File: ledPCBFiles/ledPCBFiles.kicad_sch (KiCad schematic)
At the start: 0 parts

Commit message: Added 555 timer
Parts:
- added R1: 10k, symbol Device:R
- added U1: LM555xN, Package_DIP:DIP-8_W7.62mm, symbol Timer:LM555xN
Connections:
- new net +6V: U1.8 (VCC)
- new net GND: U1.1 (GND)
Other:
- title: (none) -> Schematic for 4-Bit LED Counter

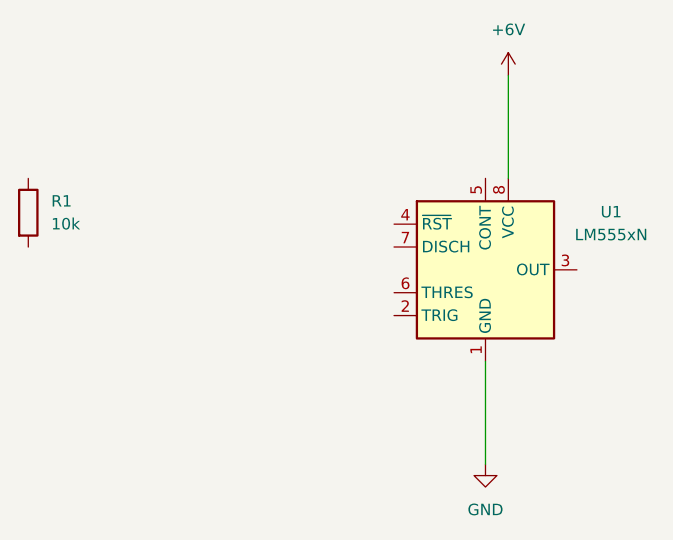
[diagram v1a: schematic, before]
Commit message: Added 100 nF capacitor to pin 5 on 555 timer
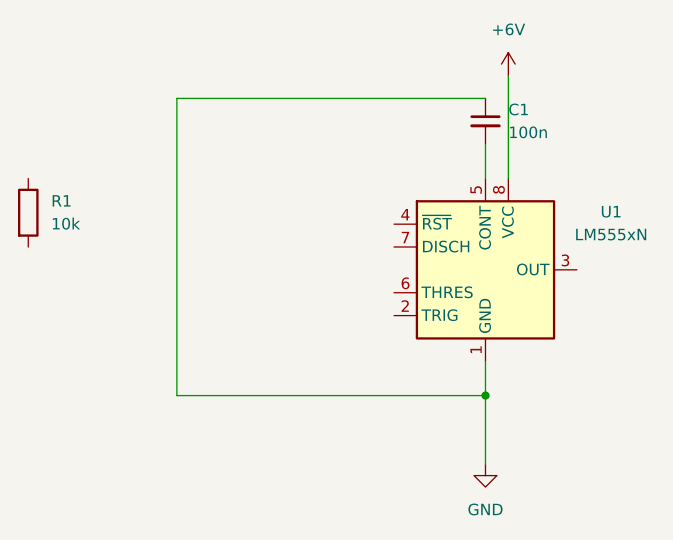
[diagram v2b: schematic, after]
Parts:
- added C1: 100n, symbol Device:C_Small
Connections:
- net GND: now also C1.1
- net at U1.5 (CONT): now also C1.2
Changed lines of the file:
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@@
 		(date "2026-06-07")
 	)
-	(wire
-		(pts
-			(xy 119.38 93.98) (xy 119.38 105.41)
+	(junction
+		(at 119.38 97.79)
+		(diameter 0)
+		(color 0 0 0 0)
+	)
+	(wire
+		(pts
+			(xy 119.38 97.79) (xy 119.38 105.41)
+		)
+		(stroke
+			(width 0)
+			(type default)
+		)
+	)
+	(wire
+		(pts
+			(xy 85.09 97.79) (xy 119.38 97.79)
+		)
+		(stroke
+			(width 0)
+			(type default)
+		)
+	)
+	(wire
+		(pts
+			(xy 85.09 64.77) (xy 85.09 97.79)
+		)
+		(stroke
+			(width 0)
+			(type default)
+		)
+	)
+	(wire
+		(pts
+			(xy 119.38 64.77) (xy 85.09 64.77)
+		)
+		(stroke
+			(width 0)
+			(type default)
+		)
+	)
+	(wire
+		(pts
+			(xy 119.38 69.85) (xy 119.38 73.66)
+		)
+		(stroke
+			(width 0)
+			(type default)
+		)
+	)
+	(wire
+		(pts
+			(xy 119.38 93.98) (xy 119.38 97.79)
 		)
 		(stroke
@@
 					(unit 1)
 				)
+			)
+		)
+	)
+	(symbol
+		(lib_id "Device:C_Small")
+		(at 119.38 67.31 0)
+		(unit 1)
+		(body_style 1)
+		(exclude_from_sim no)
+		(in_bom yes)
+		(on_board yes)
+		(in_pos_files yes)
+		(dnp no)
+		(fields_autoplaced yes)
+		(property "Reference" "C1"
+			(at 121.92 66.0462 0)
+			(show_name no)
+			(do_not_autoplace no)
+			(effects
+				(font
+					(size 1.27 1.27)
+				)
+				(justify left)
+			)
+		)
+		(property "Value" "100n"
+			(at 121.92 68.5862 0)
+			(show_name no)
+			(do_not_autoplace no)
+			(effects
+				(font
+					(size 1.27 1.27)
+				)
+				(justify left)
+			)
+		)
+		(property "Footprint" ""
+			(at 119.38 67.31 0)
+			(hide yes)
+			(show_name no)
+			(do_not_autoplace no)
+			(effects
+				(font
+					(size 1.27 1.27)
+				)
+			)
+		)
+		(property "Datasheet" ""
+			(at 119.38 67.31 0)
+			(hide yes)
+			(show_name no)
+			(do_not_autoplace no)
+			(effects
+				(font
+					(size 1.27 1.27)
+				)
+			)
+		)
+		(property "Description" "Unpolarized capacitor, small symbol"
+			(at 119.38 67.31 0)
+			(hide yes)
+			(show_name no)
+			(do_not_autoplace no)
+			(effects
+				(font
+					(size 1.27 1.27)
+				)
+			)
+		)
+		(pin "2"
+		)
+		(pin "1"
+		)
+		(instances
+			(project "ledPCBFiles"
+				(path "/4f60fb88-ed3b-40be-bc71-757dad150f17"
+					(reference "C1")
+					(unit 1)
+				)

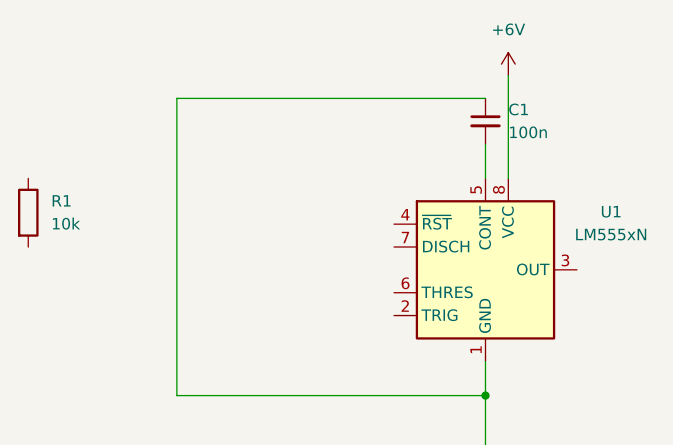
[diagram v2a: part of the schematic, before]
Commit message: Added a resistor
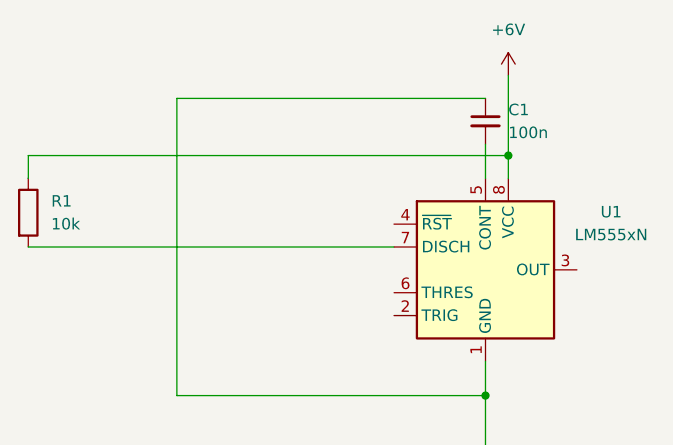
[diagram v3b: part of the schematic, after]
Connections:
- net +6V: now also R1.1
- net at U1.7 (DISCH): now also R1.2
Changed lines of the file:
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@@
+	)
+	(junction
+		(at 121.92 71.12)
+		(diameter 0)
+		(color 0 0 0 0)
 	)
 	(junction
@@
 		(diameter 0)
 		(color 0 0 0 0)
+	)
+	(wire
+		(pts
+			(xy 68.58 81.28) (xy 109.22 81.28)
+		)
+		(stroke
+			(width 0)
+			(type default)
+		)
 	)
 	(wire
@@
 		(pts
 			(xy 85.09 97.79) (xy 119.38 97.79)
+		)
+		(stroke
+			(width 0)
+			(type default)
+		)
+	)
+	(wire
+		(pts
+			(xy 68.58 73.66) (xy 68.58 71.12)
 		)
 		(stroke
@@
 	(wire
 		(pts
-			(xy 121.92 62.23) (xy 121.92 73.66)
+			(xy 68.58 71.12) (xy 121.92 71.12)
 		)
 		(stroke
+			(width 0)
+			(type default)
+		)
+	)
+	(wire
+		(pts
+			(xy 121.92 62.23) (xy 121.92 71.12)
+		)
+		(stroke
+			(width 0)
+			(type default)
+		)
+	)
+	(wire
+		(pts
+			(xy 121.92 71.12) (xy 121.92 73.66)
+		)
+		(stroke

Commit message: Removed resistor
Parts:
- removed R1: 10k, symbol Device:R
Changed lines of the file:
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@@
-	)
-	(junction
-		(at 121.92 71.12)
-		(diameter 0)
-		(color 0 0 0 0)
 	)
 	(junction
@@
 		(diameter 0)
 		(color 0 0 0 0)
-	)
-	(wire
-		(pts
-			(xy 68.58 81.28) (xy 109.22 81.28)
-		)
-		(stroke
-			(width 0)
-			(type default)
-		)
 	)
 	(wire
@@
 		(pts
 			(xy 85.09 97.79) (xy 119.38 97.79)
-		)
-		(stroke
-			(width 0)
-			(type default)
-		)
-	)
-	(wire
-		(pts
-			(xy 68.58 73.66) (xy 68.58 71.12)
 		)
 		(stroke
@@
 	(wire
 		(pts
-			(xy 68.58 71.12) (xy 121.92 71.12)
-		)
-		(stroke
-			(width 0)
-			(type default)
-		)
-	)
-	(wire
-		(pts
-			(xy 121.92 62.23) (xy 121.92 71.12)
-		)
-		(stroke
-			(width 0)
-			(type default)
-		)
-	)
-	(wire
-		(pts
-			(xy 121.92 71.12) (xy 121.92 73.66)
+			(xy 121.92 62.23) (xy 121.92 73.66)
 		)
 		(stroke
@@
 					(unit 1)
 				)
-			)
-		)
-	)
-	(symbol
-		(lib_id "Device:R")
-		(at 68.58 77.47 0)
-		(unit 1)
-		(body_style 1)
-		(exclude_from_sim no)
-		(in_bom yes)
-		(on_board yes)
-		(in_pos_files yes)
-		(dnp no)
-		(fields_autoplaced yes)
-		(property "Reference" "R1"
-			(at 71.12 76.1999 0)
-			(show_name no)
-			(do_not_autoplace no)
-			(effects
-				(font
-					(size 1.27 1.27)
-				)
-				(justify left)
-			)
-		)
-		(property "Value" "10k"
-			(at 71.12 78.7399 0)
-			(show_name no)
-			(do_not_autoplace no)
-			(effects
-				(font
-					(size 1.27 1.27)
-				)
-				(justify left)
-			)
-		)
-		(property "Footprint" ""
-			(at 66.802 77.47 90)
-			(hide yes)
-			(show_name no)
-			(do_not_autoplace no)
-			(effects
-				(font
-					(size 1.27 1.27)
-				)
-			)
-		)
-		(property "Datasheet" ""
-			(at 68.58 77.47 0)
-			(hide yes)
-			(show_name no)
-			(do_not_autoplace no)
-			(effects
-				(font
-					(size 1.27 1.27)
-				)
-			)
-		)
-		(property "Description" "Resistor"
-			(at 68.58 77.47 0)
-			(hide yes)
-			(show_name no)
-			(do_not_autoplace no)
-			(effects
-				(font
-					(size 1.27 1.27)
-				)
-			)
-		)
-		(pin "2"
-		)
-		(pin "1"
-		)
-		(instances
-			(project "ledPCBFiles"
-				(path "/4f60fb88-ed3b-40be-bc71-757dad150f17"
-					(reference "R1")
-					(unit 1)
-				)

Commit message: added a resistor
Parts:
- added R1: 10k, symbol Device:R_US
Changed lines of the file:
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@@
+	)
+	(symbol
+		(lib_id "Device:R_US")
+		(at 69.85 76.2 0)
+		(unit 1)
+		(body_style 1)
+		(exclude_from_sim no)
+		(in_bom yes)
+		(on_board yes)
+		(in_pos_files yes)
+		(dnp no)
+		(fields_autoplaced yes)
+		(property "Reference" "R1"
+			(at 72.39 74.9299 0)
+			(show_name no)
+			(do_not_autoplace no)
+			(effects
+				(font
+					(size 1.27 1.27)
+				)
+				(justify left)
+			)
+		)
+		(property "Value" "10k"
+			(at 72.39 77.4699 0)
+			(show_name no)
+			(do_not_autoplace no)
+			(effects
+				(font
+					(size 1.27 1.27)
+				)
+				(justify left)
+			)
+		)
+		(property "Footprint" ""
+			(at 70.866 76.454 90)
+			(hide yes)
+			(show_name no)
+			(do_not_autoplace no)
+			(effects
+				(font
+					(size 1.27 1.27)
+				)
+			)
+		)
+		(property "Datasheet" ""
+			(at 69.85 76.2 0)
+			(hide yes)
+			(show_name no)
+			(do_not_autoplace no)
+			(effects
+				(font
+					(size 1.27 1.27)
+				)
+			)
+		)
+		(property "Description" "Resistor, US symbol"
+			(at 69.85 76.2 0)
+			(hide yes)
+			(show_name no)
+			(do_not_autoplace no)
+			(effects
+				(font
+					(size 1.27 1.27)
+				)
+			)
+		)
+		(pin "1"
+		)
+		(pin "2"
+		)
+		(instances
+			(project "ledPCBFiles"
+				(path "/4f60fb88-ed3b-40be-bc71-757dad150f17"
+					(reference "R1")
+					(unit 1)
+				)
+			)
+		)
 	)
 	(symbol

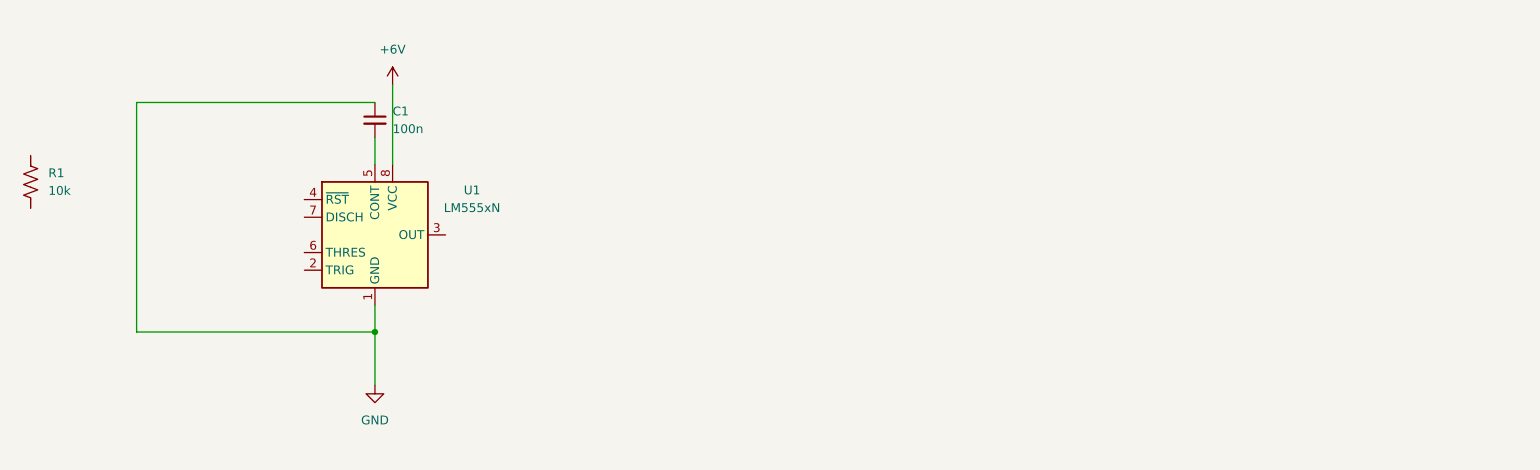
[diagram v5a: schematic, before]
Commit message: Added resistors and LEDs to 74LS161 counter
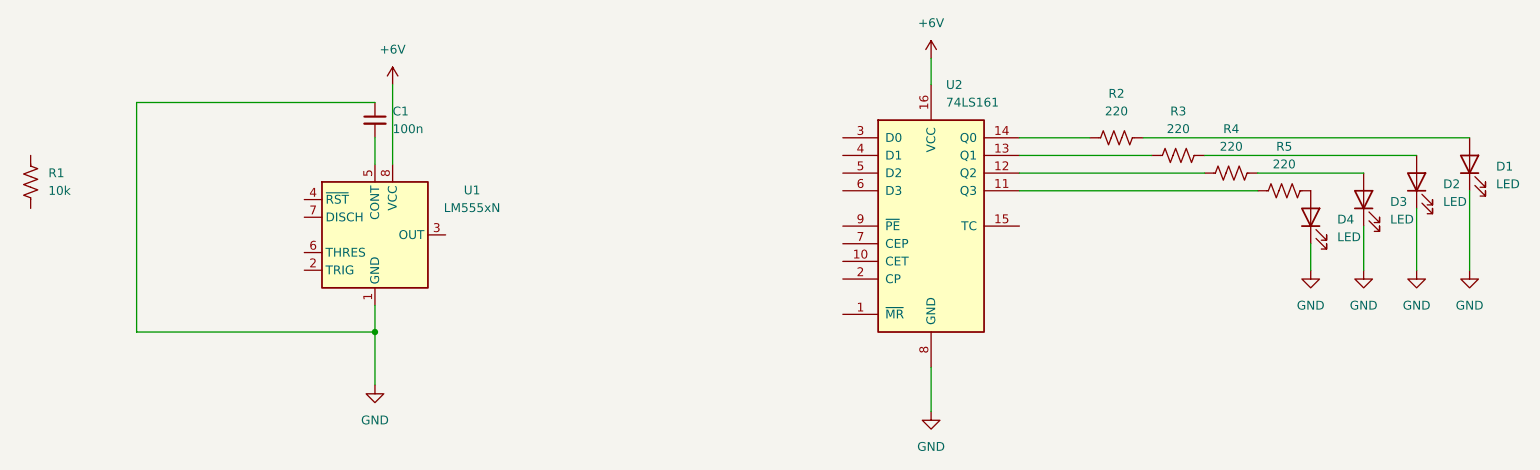
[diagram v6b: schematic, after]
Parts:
- added D1, D2, D3, D4: LED, symbol Device:LED
- added R2, R3, R4, R5: 220, symbol Device:R_US
- added U2: 74LS161, symbol 74xx:74LS161
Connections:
- net +6V: now also U2.16 (VCC)
- net GND: now also D1.1 (K), D2.1 (K), D3.1 (K), D4.1 (K), U2.8 (GND)
- new net: D3.2 (A), R4.2
- new net: R4.1, U2.12 (Q2)
- new net: D1.2 (A), R2.2
- new net: D2.2 (A), R3.2
- new net: R2.1, U2.14 (Q0)
- new net: R5.1, U2.11 (Q3)
- new net: D4.2 (A), R5.2
- new net: R3.1, U2.13 (Q1)

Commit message: Added voltages to counter
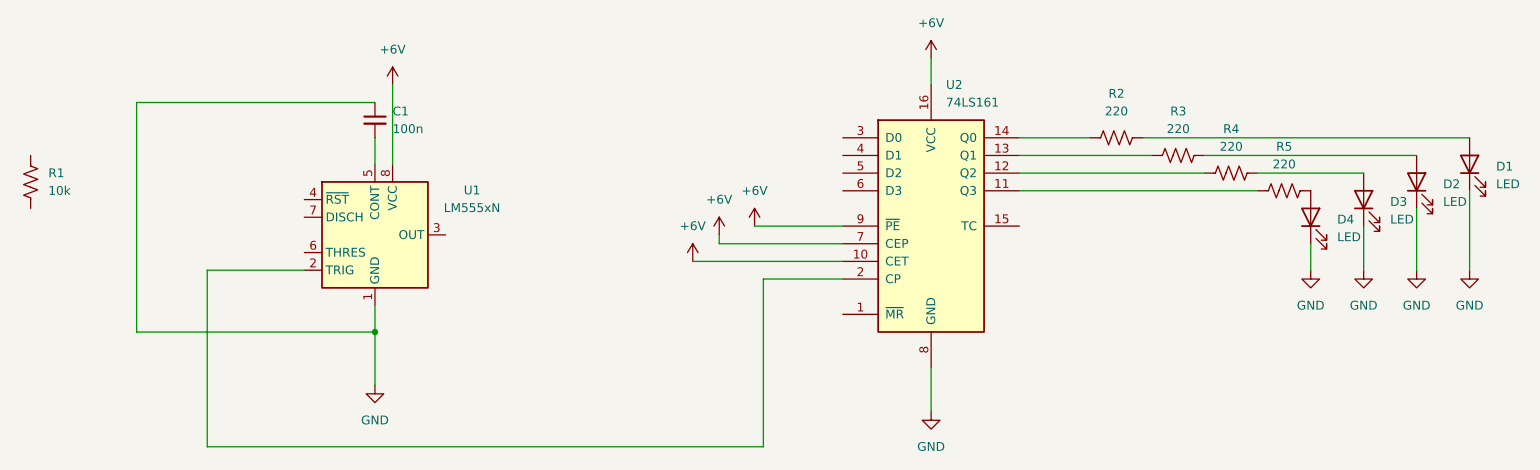
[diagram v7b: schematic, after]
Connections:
- net +6V: now also U2.10 (CET), U2.7 (CEP), U2.9 (~{PE})
- net at U1.2 (TRIG): now also U2.2 (CP)

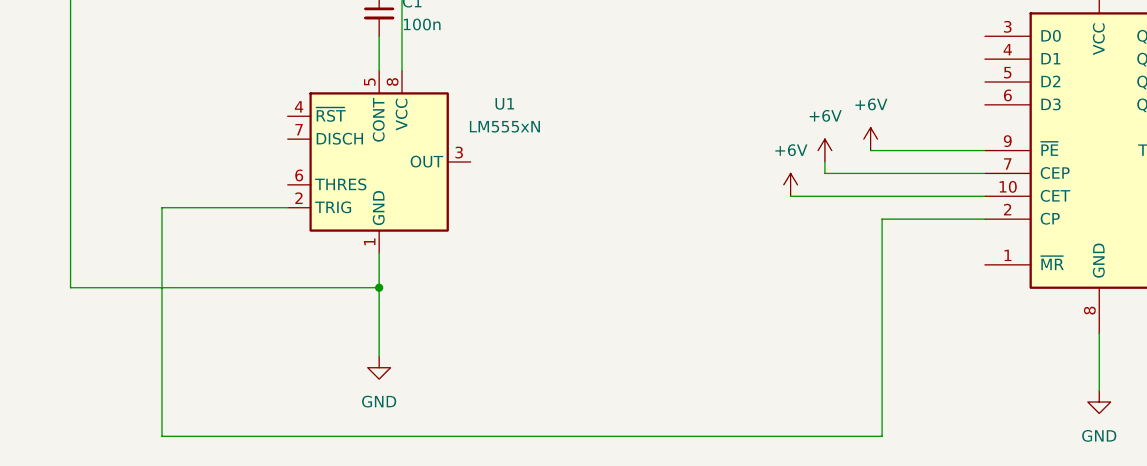
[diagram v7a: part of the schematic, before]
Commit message: Changes connection from pin 3 on 555 timer to pin 2 on 74LS161
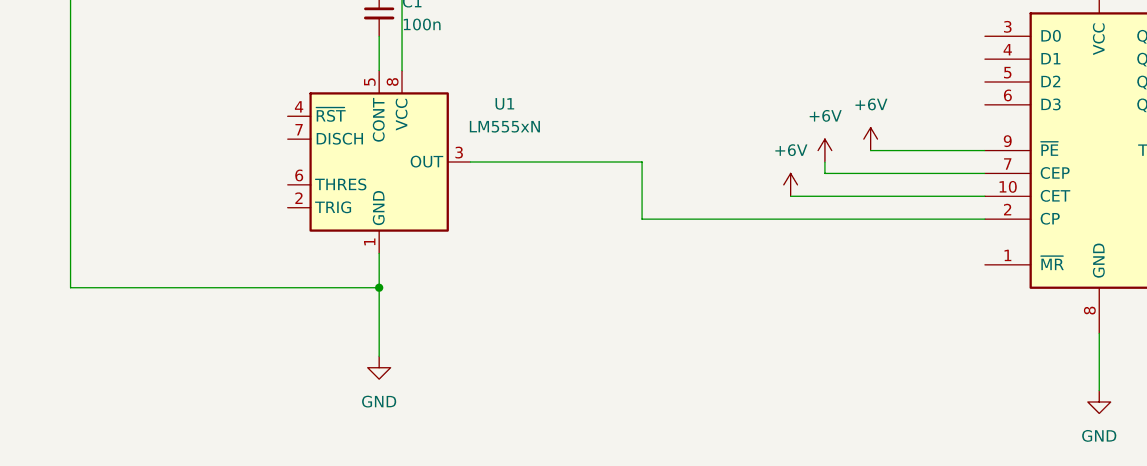
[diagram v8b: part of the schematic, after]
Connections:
- net at U1.2 (TRIG): no longer U2.2 (CP)
- net at U1.3 (OUT): now also U2.2 (CP)
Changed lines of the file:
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@@
-	(wire
-		(pts
-			(xy 95.25 88.9) (xy 95.25 114.3)
-		)
-		(stroke
-			(width 0)
-			(type default)
-		)
-	)
-	(wire
-		(pts
-			(xy 95.25 114.3) (xy 175.26 114.3)
-		)
-		(stroke
-			(width 0)
-			(type default)
-		)
-	)
-	(wire
-		(pts
-			(xy 175.26 90.17) (xy 186.69 90.17)
-		)
-		(stroke
-			(width 0)
-			(type default)
-		)
-	)
 	(wire
 		(pts
@@
 	(wire
 		(pts
+			(xy 129.54 83.82) (xy 148.59 83.82)
+		)
+		(stroke
+			(width 0)
+			(type default)
+		)
+	)
+	(wire
+		(pts
 			(xy 269.24 80.01) (xy 269.24 88.9)
 		)
@@
 	(wire
 		(pts
-			(xy 109.22 88.9) (xy 95.25 88.9)
+			(xy 148.59 90.17) (xy 186.69 90.17)
+		)
+		(stroke
+			(width 0)
+			(type default)
+		)
+	)
+	(wire
+		(pts
+			(xy 148.59 83.82) (xy 148.59 90.17)
 		)
 		(stroke
@@
 		)
 		(stroke
-			(width 0)
-			(type default)
-		)
-	)
-	(wire
-		(pts
-			(xy 175.26 114.3) (xy 175.26 90.17)
-		)
-		(stroke
